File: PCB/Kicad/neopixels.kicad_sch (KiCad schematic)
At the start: 44 parts

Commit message: more routing
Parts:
- C1, C10, C11, C12, C13, C14, C15, C16, C17, C18, C19, C2, C20, C21, C3, C4, C5, C6, C7, C8, C9: footprint Capacitor_SMD:C_1206_3216Metric_Pad1.33x1.80mm_HandSolder -> Library:C_1206_3216Metric_Pad1.33x1.80mm_HandSolder
- NP1, NP10, NP11, NP12, NP13, NP14, NP15, NP16, NP17, NP18, NP19, NP2, NP20, NP21, NP3, NP4, NP5, NP6, NP7, NP8, NP9: footprint LED_SMD:LED_WS2812B_PLCC4_5.0x5.0mm_P3.2mm -> Library:LED_WS2812B_PLCC4_5.0x5.0mm_P3.2mm

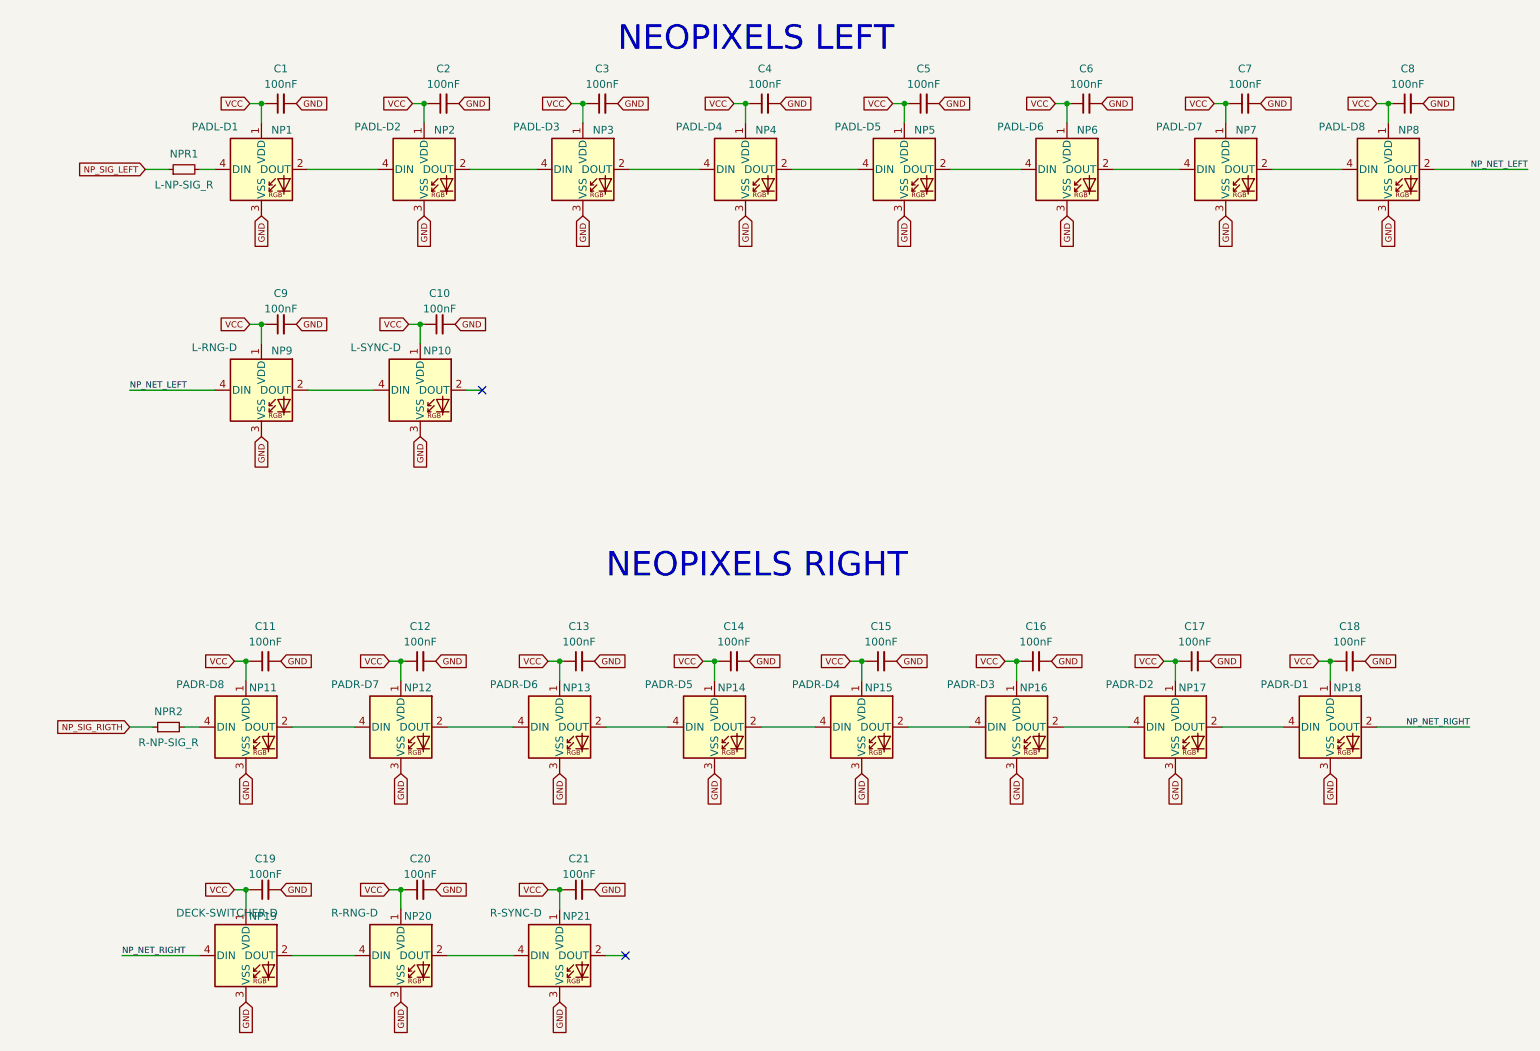
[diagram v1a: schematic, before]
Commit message: removed neopixel capacitors
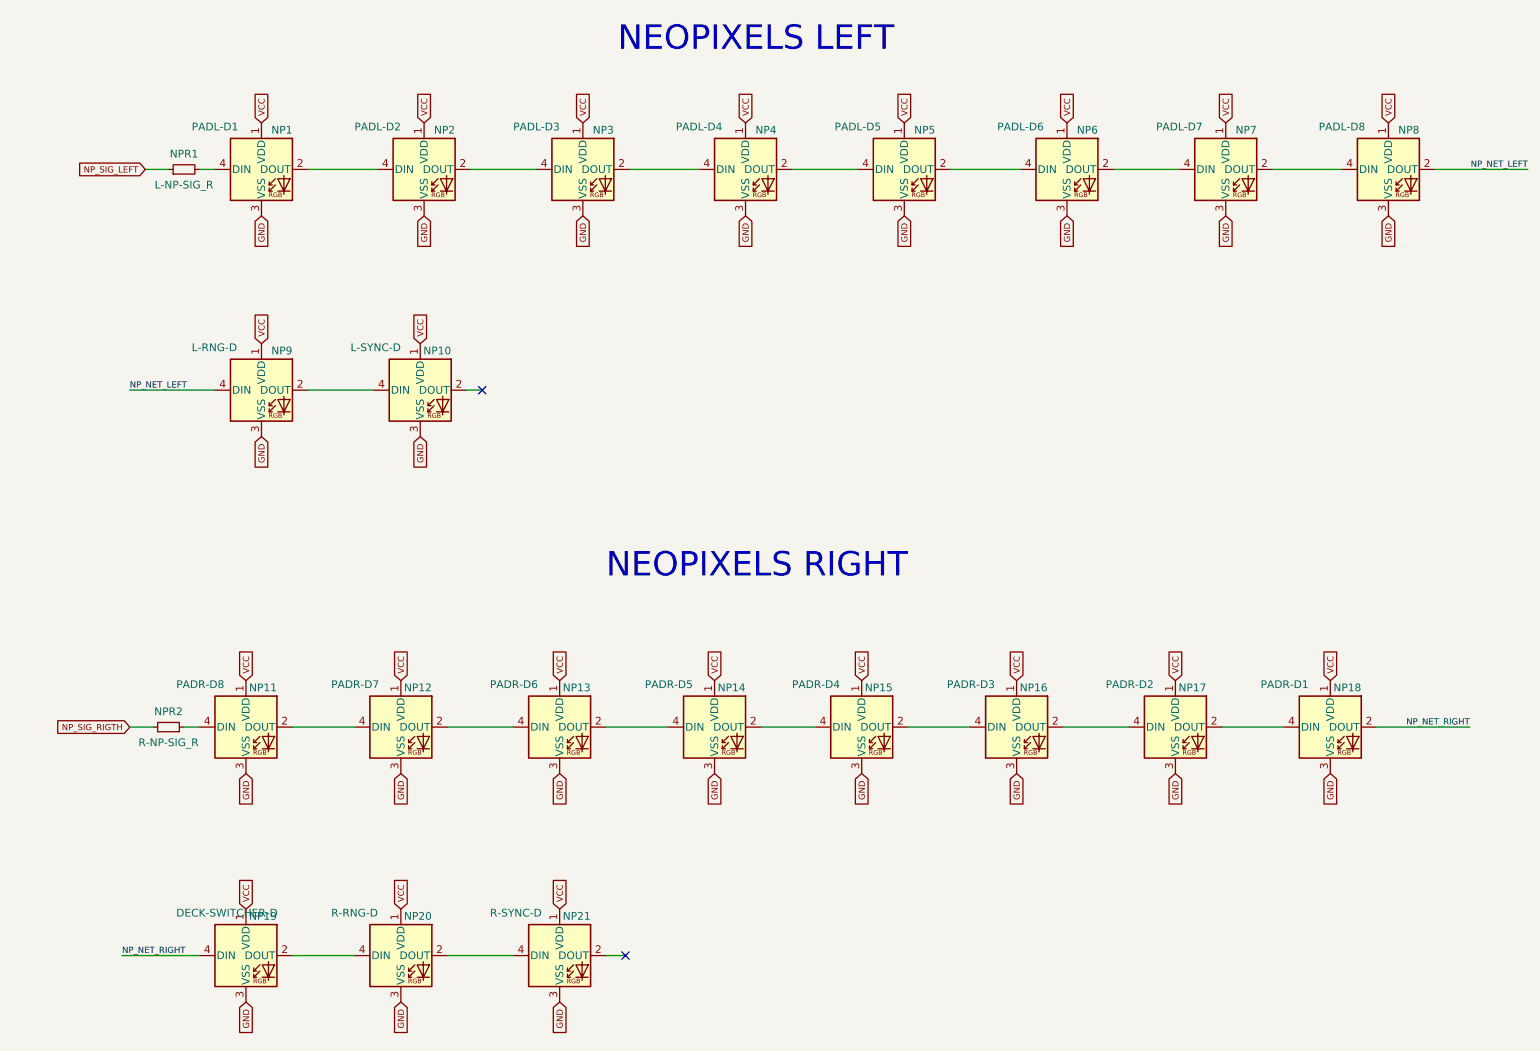
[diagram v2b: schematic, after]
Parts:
- removed C1, C10, C11, C12, C13, C14, C15, C16, C17, C18, C19, C2, C20, C21, C3, C4, C5, C6, C7, C8, C9: 100nF, Library:C_1206_3216Metric_Pad1.33x1.80mm_HandSolder, symbol Device:C_Small

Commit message: schematic updated
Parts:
- added NPR3: L-NP-FB_R, Library:R_1206_3216Metric_Pad1.30x1.75mm_HandSolder, symbol Device:R_Small
- added NPR4: R-NP-FB_R, Library:R_1206_3216Metric_Pad1.30x1.75mm_HandSolder, symbol Device:R_Small
- NPR1: value L-NP-SIG_R -> L-NP-PADS_R
- NPR2: value R-NP-SIG_R -> R-NP-PADS_R
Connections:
- net NP_NET_RIGHT: no longer NP19.4 (DIN)
- net NP_NET_LEFT: no longer names the net of NP9.4 (DIN)
- net NP_NET_LEFT: now also NPR3.2; no longer NP8.2 (DOUT)
- net NP_SIG_LEFT renamed NP_L_PADS_DATA
- net NP_SIG_RIGTH renamed NP_R_PADS_DATA
- new net: NP19.4 (DIN), NPR4.2
- new net NP_L_FB_DATA: NPR3.1
- new net NP_R_FB_DATA: NPR4.1
- no-connect marks 2 -> 3

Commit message: schematic updated
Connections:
- net at NP13.2 (DOUT): now also NP12.4 (DIN); no longer NP14.4 (DIN)
- net at NP13.4 (DIN): now also NP14.2 (DOUT); no longer NP12.2 (DOUT)
- net at NP16.2 (DOUT): now also NP15.4 (DIN); no longer NP17.4 (DIN)
- net at NP16.4 (DIN): now also NP17.2 (DOUT); no longer NP15.2 (DOUT)
- net at NPR2.2: now also NP18.4 (DIN); no longer NP11.4 (DIN)
- net at NP11.2 (DOUT): no longer NP12.4 (DIN)
- net NP_NET_RIGHT: no longer names the net of NP18.2 (DOUT)
- net NP_NET_RIGHT: now also NP17.4 (DIN)
- new net: NP14.4 (DIN), NP15.2 (DOUT)
- new net: NP11.4 (DIN), NP12.2 (DOUT)
- no-connect marks 3 -> 4
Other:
- moved on the sheet: NP11, NP12, NP13, NP14, NP15, NP16, NP17, NP18

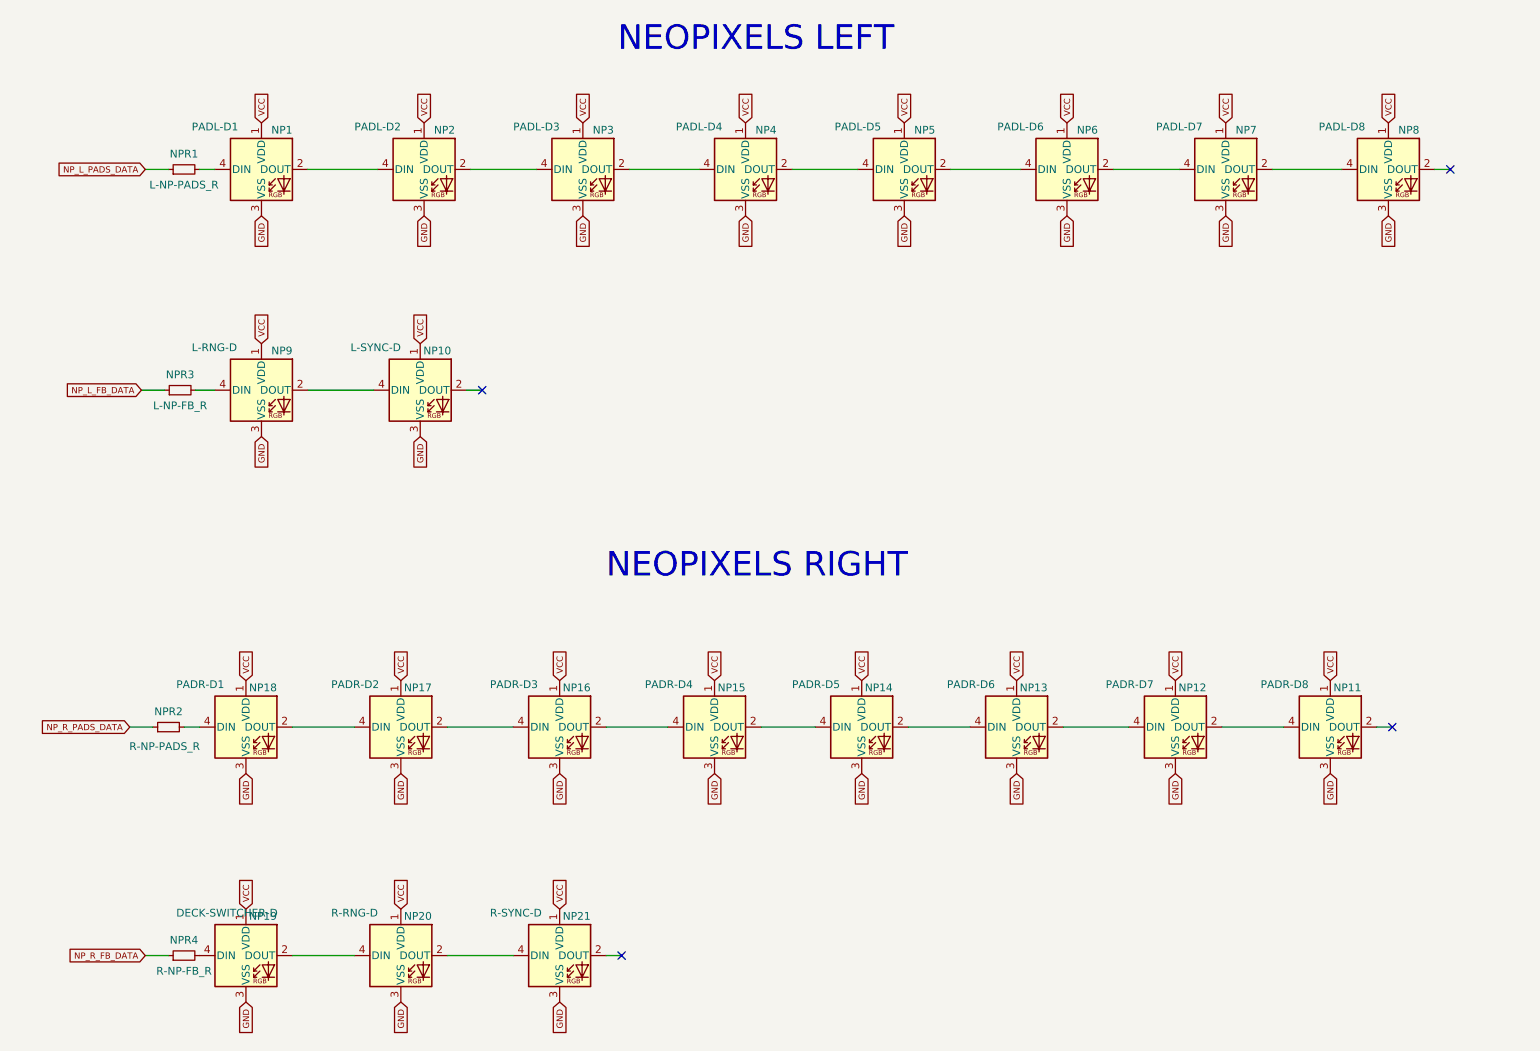
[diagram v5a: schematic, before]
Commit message: all neopixels together
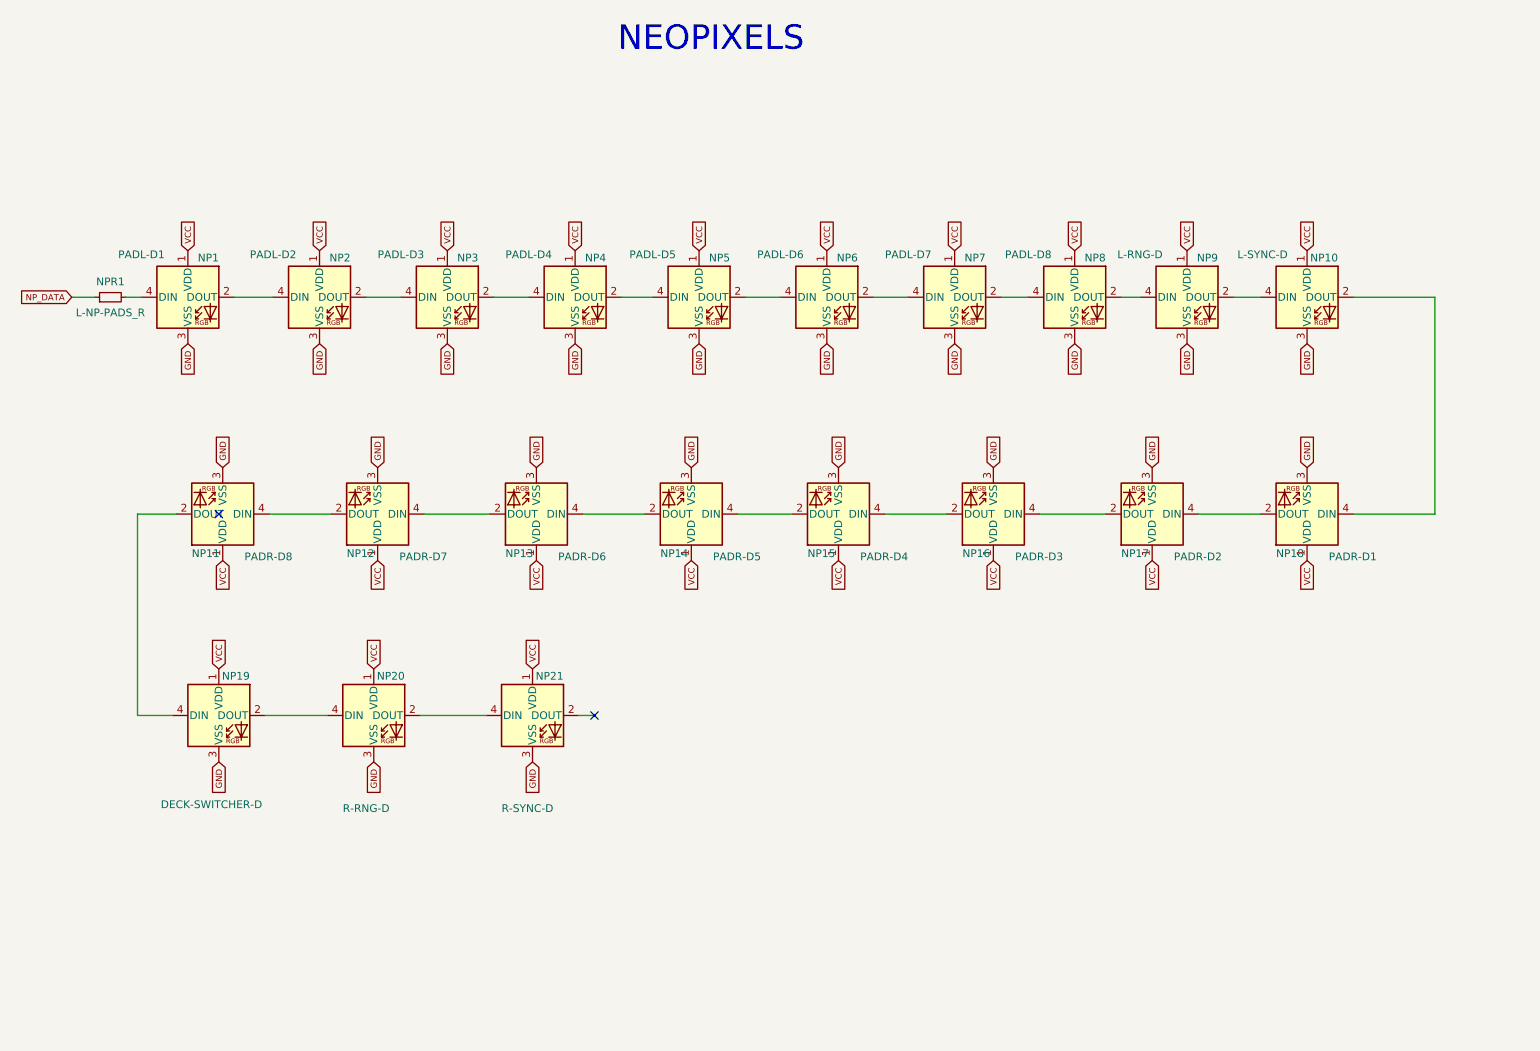
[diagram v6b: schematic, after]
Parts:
- removed NPR2: R-NP-PADS_R, Library:R_1206_3216Metric_Pad1.30x1.75mm_HandSolder, symbol Device:R_Small
- removed NPR3: L-NP-FB_R, Library:R_1206_3216Metric_Pad1.30x1.75mm_HandSolder, symbol Device:R_Small
- removed NPR4: R-NP-FB_R, Library:R_1206_3216Metric_Pad1.30x1.75mm_HandSolder, symbol Device:R_Small
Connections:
- net at NP19.4 (DIN): now also NP11.2 (DOUT)
- net at NP9.4 (DIN): now also NP8.2 (DOUT)
- net at NP10.2 (DOUT): now also NP18.4 (DIN)
- net NP_L_PADS_DATA renamed NP_DATA
- no-connect marks 4 -> 2
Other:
- note added: "NEOPIXELS"
- note removed: "NEOPIXELS LEFT"
- note removed: "NEOPIXELS RIGHT"
- moved on the sheet: NP1, NP10, NP11, NP12, NP13, NP14, NP15, NP16, NP17, NP18, NP19, NP2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

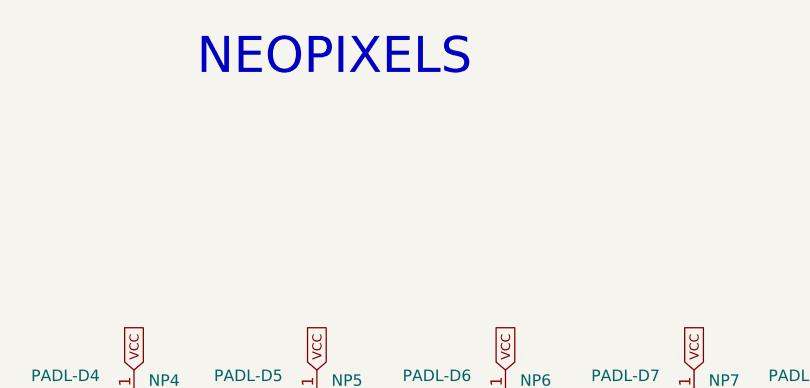
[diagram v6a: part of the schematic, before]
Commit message: changed encoders pins to interrupt pins
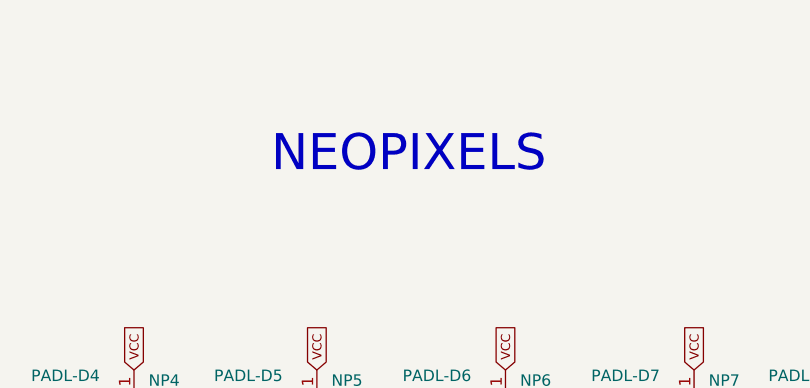
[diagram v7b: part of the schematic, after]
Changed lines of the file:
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@@
     (stroke (width 0) (type solid) (color 0 0 0 0))
   )
-  (text "NEOPIXELS" (at 114.3 24.13 0)
+  (text "NEOPIXELS" (at 122.555 34.925 0)
     (effects (font (size 4 4)) (justify left bottom))
   )
